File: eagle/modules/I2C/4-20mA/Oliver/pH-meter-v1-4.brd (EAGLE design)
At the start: 113 x 82.5 mm, 42 parts, among them IC1 CA3140N, IC2 TL081P, IC3 ICL7660CPA, IC4 7805L, J2 I2C, J3 I2C, X1 BTOR1

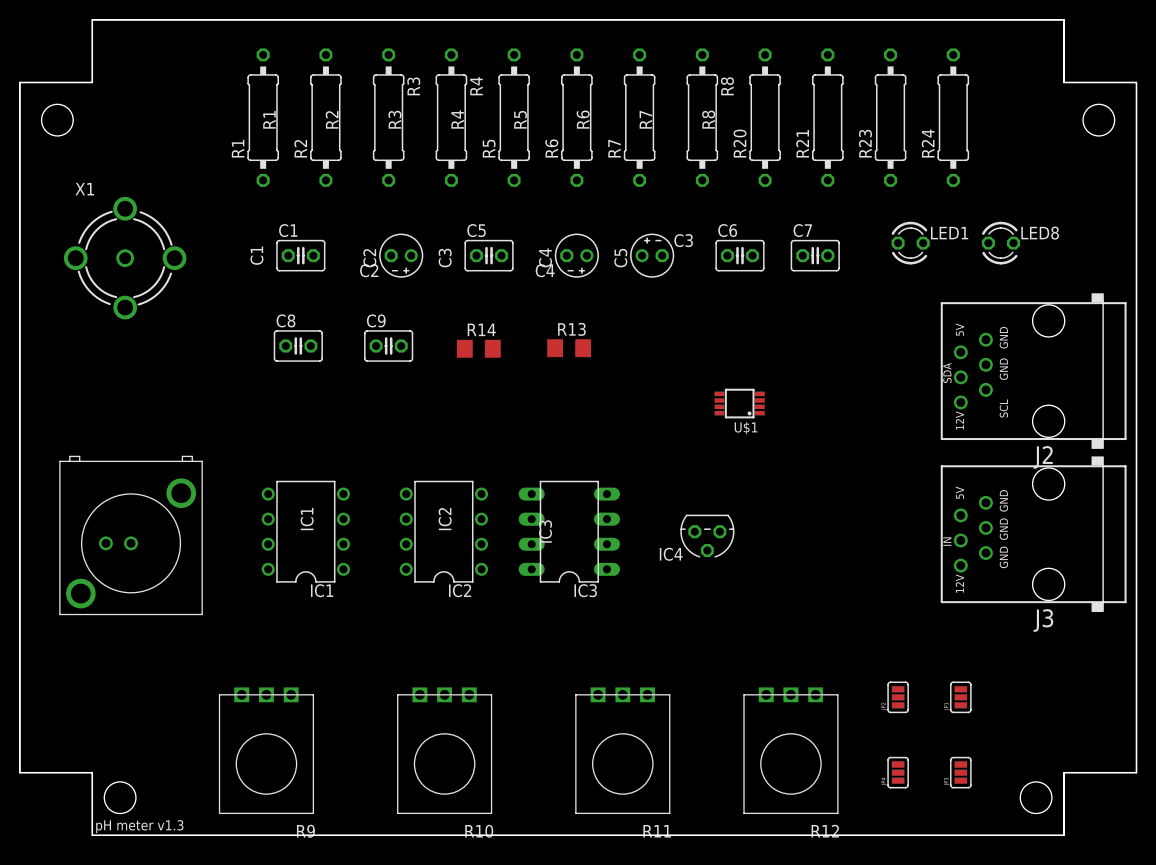
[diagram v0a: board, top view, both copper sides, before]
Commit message: pH meter Eagle schematics and PCB files (routed)
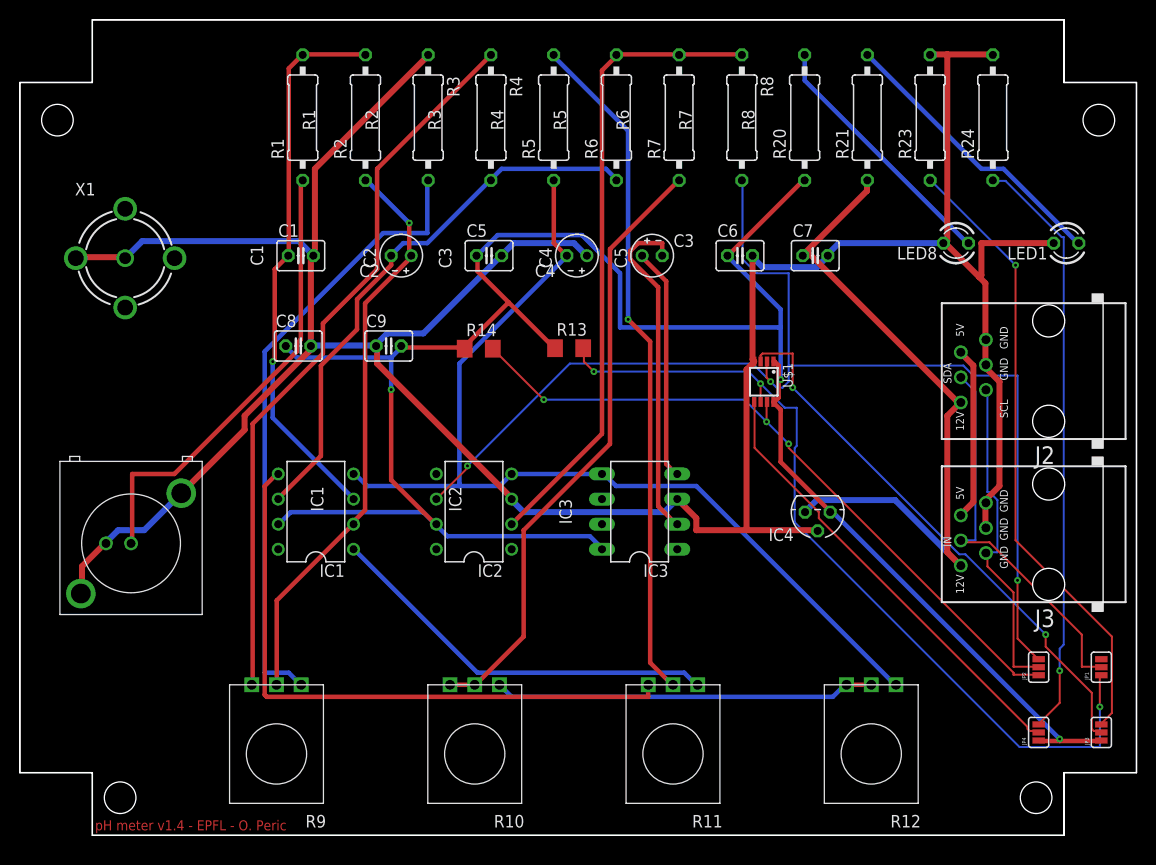
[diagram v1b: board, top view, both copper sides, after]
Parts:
- moved LED1 15.7 mm to (105.9, 59.9), turned to 180 degrees
- moved JP3 14.8 mm to (109.5, 10.4)
- moved JP4 14.8 mm to (103.1, 10.4)
- moved JP1 14.5 mm to (109.5, 17.0)
- moved JP2 14.5 mm to (103.1, 17.0)
- moved IC4 11.3 mm to (80.8, 32.7)
- moved R12 8.19 mm to (90.9, 15.2)
- moved IC3 7.40 mm to (62.7, 32.8)
- moved R11 5.18 mm to (70.9, 15.2)
- moved LED8 4.56 mm to (94.8, 59.9), turned to 180 degrees
- moved R1 4.00 mm to (28.6, 72.6)
- moved R2 4.00 mm to (35.0, 72.6)
- moved R20 4.00 mm to (79.4, 72.6)
- moved R21 4.00 mm to (85.8, 72.6)
- moved R23 4.00 mm to (92.1, 72.6)
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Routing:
- net GND: track 0.00 -> 302.1 mm
- net +5V: track 0.00 -> 214.4 mm, vias 0 -> 3
- net DATA_OUT: track 0.00 -> 122.4 mm, vias 0 -> 3
- net -5V: track 0.00 -> 100.7 mm
- net N$14: track 0.00 -> 86.0 mm, vias 0 -> 3
- net N$7: track 0.00 -> 73.8 mm
- net N$15: track 0.00 -> 71.3 mm, vias 0 -> 3
- net +12V: track 0.00 -> 69.3 mm
- net N$3: track 0.00 -> 68.8 mm, vias 0 -> 1
- net N$12: track 0.00 -> 64.6 mm
- net ASDF: track 0.00 -> 63.5 mm
- net N$18: track 0.00 -> 63.1 mm, vias 0 -> 1
- net N$4: track 0.00 -> 63.1 mm
- net N$8: track 0.00 -> 62.2 mm
- net N$19: track 0.00 -> 59.9 mm, vias 0 -> 1
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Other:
- board text added: "pH meter v1.4 - EPFL - O. Peric"
- board text removed: "pH meter v1.3"

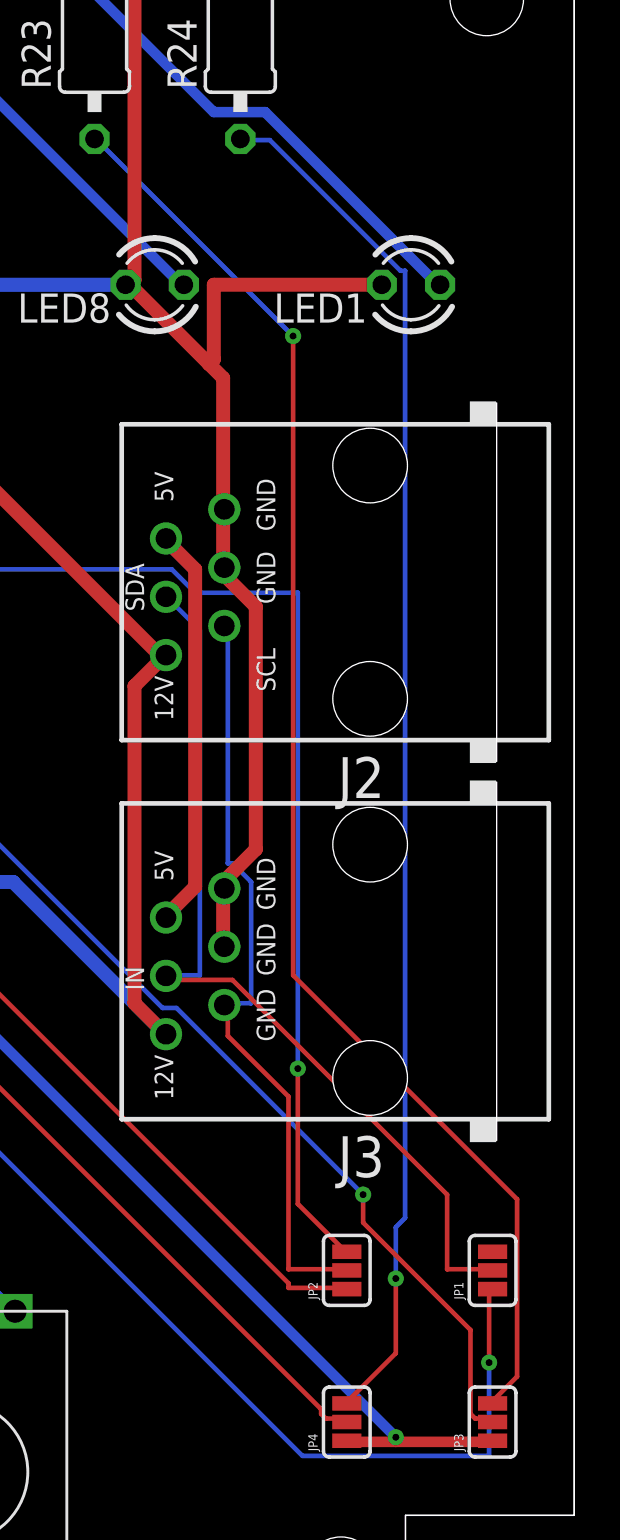
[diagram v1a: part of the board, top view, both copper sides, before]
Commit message: pH-meter 1.4 Eagle schematics and PCB files (routed) bugfix for hole though signal line.
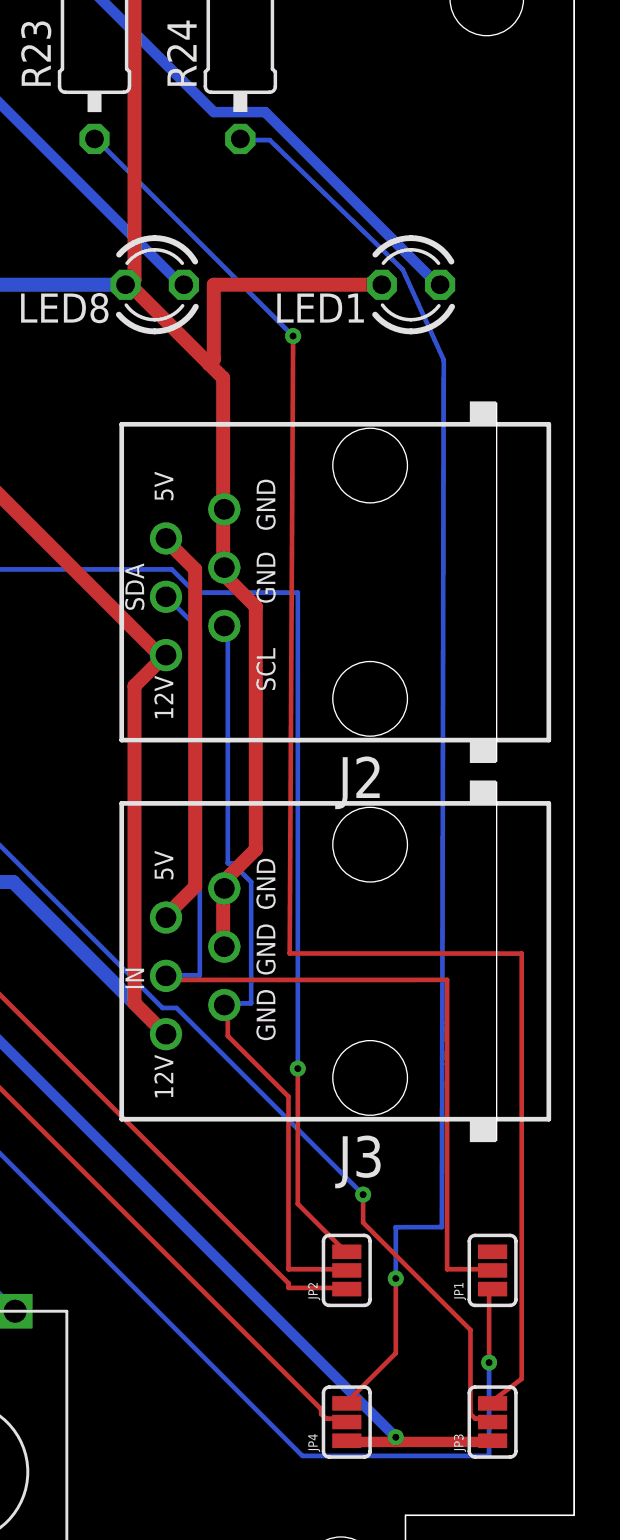
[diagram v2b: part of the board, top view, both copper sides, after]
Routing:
- net N$18: track 63.1 -> 69.4 mm
- net SDA: track 40.1 -> 45.6 mm
- net N$19: track 59.9 -> 62.0 mm
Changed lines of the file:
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@@
 <?xml version="1.0" encoding="utf-8"?>
 <!DOCTYPE eagle SYSTEM "eagle.dtd">
-<eagle version="6.1">
+<eagle version="6.2">
 <drawing>
 <settings>
@@
 <setting verticaltext="up"/>
 </settings>
-<grid distance="1" unitdist="mm" unit="mm" style="lines" multiple="1" display="yes" altdistance="0.1" altunitdist="mm" altunit="mm"/>
+<grid distance="1" unitdist="mm" unit="mm" style="lines" multiple="1" display="yes" altdistance="0.05" altunitdist="mm" altunit="mm"/>
 <layers>
 <layer number="1" name="Top" color="4" fill="1" visible="yes" active="yes"/>
@@
 <contactref element="J2" pad="SDA"/>
 <wire x1="107.4928" y1="17.0688" x2="109.3216" y2="17.0688" width="0.2032" layer="1"/>
-<wire x1="107.4928" y1="20.32" x2="107.4928" y2="17.0688" width="0.2032" layer="1"/>
-<wire x1="98.1456" y1="29.6672" x2="107.4928" y2="20.32" width="0.2032" layer="1"/>
-<wire x1="95.3008" y1="29.6672" x2="98.1456" y2="29.6672" width="0.2032" layer="1"/>
+<wire x1="107.4928" y1="29.67" x2="107.4928" y2="17.0688" width="0.2032" layer="1"/>
+<wire x1="100.1456" y1="29.6672" x2="107.4928" y2="29.67" width="0.2032" layer="1"/>
+<wire x1="95.3008" y1="29.6672" x2="100.1456" y2="29.6672" width="0.2032" layer="1"/>
 <wire x1="109.3216" y1="17.0688" x2="109.474" y2="17.018" width="0.2032" layer="1"/>
 <wire x1="95.3008" y1="29.6672" x2="95.25" y2="29.845" width="0.2032" layer="1"/>
@@
 <contactref element="JP3" pad="3"/>
 <contactref element="R23" pad="1"/>
-<wire x1="110.5408" y1="12.3952" x2="109.5248" y2="11.3792" width="0.2032" layer="1"/>
-<wire x1="110.5408" y1="20.1168" x2="110.5408" y2="12.3952" width="0.2032" layer="1"/>
-<wire x1="100.7872" y1="29.8704" x2="110.5408" y2="20.1168" width="0.2032" layer="1"/>
-<wire x1="100.7872" y1="57.7088" x2="100.7872" y2="29.8704" width="0.2032" layer="1"/>
+<wire x1="110.7408" y1="12.2952" x2="109.5248" y2="11.3792" width="0.2032" layer="1"/>
+<wire x1="110.7408" y1="30.8168" x2="110.7408" y2="12.2952" width="0.2032" layer="1"/>
+<wire x1="100.6372" y1="30.8204" x2="110.7408" y2="30.8168" width="0.2032" layer="1"/>
+<wire x1="100.7872" y1="57.7088" x2="100.6372" y2="30.8204" width="0.2032" layer="1"/>
 <wire x1="92.2528" y1="66.2432" x2="100.7872" y2="57.7088" width="0.2032" layer="16"/>
 <wire x1="109.5248" y1="11.3792" x2="109.474" y2="11.2268" width="0.2032" layer="1"/>
@@
 <wire x1="105.2576" y1="16.6624" x2="105.2576" y2="13.4112" width="0.2032" layer="1"/>
 <wire x1="105.2576" y1="18.8976" x2="105.2576" y2="16.6624" width="0.2032" layer="16"/>
-<wire x1="105.664" y1="19.304" x2="105.2576" y2="18.8976" width="0.2032" layer="16"/>
-<wire x1="105.664" y1="60.5536" x2="105.664" y2="19.304" width="0.2032" layer="16"/>
-<wire x1="105.4608" y1="60.5536" x2="105.664" y2="60.5536" width="0.2032" layer="16"/>
-<wire x1="99.7712" y1="66.2432" x2="105.4608" y2="60.5536" width="0.2032" layer="16"/>
+<wire x1="107.264" y1="18.904" x2="105.2576" y2="18.8976" width="0.2032" layer="16"/>
+<wire x1="107.3464" y1="56.664" x2="107.264" y2="18.904" width="0.2032" layer="16"/>
+<wire x1="105.5608" y1="60.6036" x2="107.3464" y2="56.664" width="0.2032" layer="16"/>
+<wire x1="99.7712" y1="66.2432" x2="105.5608" y2="60.6036" width="0.2032" layer="16"/>
 <wire x1="98.552" y1="66.2432" x2="99.7712" y2="66.2432" width="0.2032" layer="16"/>
 <wire x1="103.2256" y1="11.3792" x2="103.124" y2="11.2268" width="0.2032" layer="1"/>
